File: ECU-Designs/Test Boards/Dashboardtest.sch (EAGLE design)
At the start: 22 parts, among them X2 MINIFIT_5566-6, X3 MINIFIT_5566-10

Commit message: Revisions made courtesy of Nathan.
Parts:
- removed X3: MINIFIT_5566-10, HyTechDevices:MINIFIT_5566-10
- added X1: MINIFIT_5566-8, HyTechDevices:MINIFIT_5566-8
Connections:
- net 20: now also X1-7.S; no longer X3-8.S
- net N$13: now also X1-6.S; no longer X3-6.S
- net N$3: now also X1-1.S; no longer X3-1.S
- net N$5: now also X1-2.S; no longer X3-2.S
- net N$6: now also X1-3.S; no longer X3-3.S
- net N$7: now also X1-4.S; no longer X3-4.S
- net N$8: now also X1-8.S; no longer X3-9.S
- net N$9: now also X1-5.S; no longer X3-5.S
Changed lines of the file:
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@@
 <part name="X2" library="HyTechDevices" deviceset="MINIFIT_5566-6" device=""/>
 <part name="GND6" library="supply1" deviceset="GND" device=""/>
-<part name="X3" library="HyTechDevices" deviceset="MINIFIT_5566-10" device=""/>
 <part name="BUZZER" library="HyTechDevices" deviceset="MINIFIT_5566-2" device=""/>
 <part name="GND7" library="supply1" deviceset="GND" device=""/>
 <part name="GND5" library="supply1" deviceset="GND" device=""/>
+<part name="X1" library="HyTechDevices" deviceset="MINIFIT_5566-8" device=""/>
 </parts>
 <sheets>
@@
 <instance part="X2" gate="-6" x="-27.94" y="10.16" rot="R180"/>
 <instance part="GND6" gate="1" x="-17.78" y="10.16" rot="R90"/>
-<instance part="X3" gate="-1" x="15.24" y="53.34" rot="R90"/>
-<instance part="X3" gate="-2" x="17.78" y="53.34" rot="R90"/>
-<instance part="X3" gate="-3" x="20.32" y="53.34" rot="R90"/>
-<instance part="X3" gate="-4" x="22.86" y="53.34" rot="R90"/>
-<instance part="X3" gate="-5" x="25.4" y="53.34" rot="R90"/>
-<instance part="X3" gate="-6" x="27.94" y="53.34" rot="R90"/>
-<instance part="X3" gate="-7" x="30.48" y="53.34" rot="R90"/>
-<instance part="X3" gate="-8" x="33.02" y="53.34" rot="R90"/>
-<instance part="X3" gate="-9" x="35.56" y="58.42" rot="R90"/>
-<instance part="X3" gate="-10" x="38.1" y="58.42" rot="R90"/>
 <instance part="BUZZER" gate="-2" x="76.2" y="50.8"/>
 <instance part="BUZZER" gate="-1" x="76.2" y="53.34"/>
 <instance part="GND7" gate="1" x="55.88" y="40.64" rot="R180"/>
 <instance part="GND5" gate="1" x="48.26" y="-25.4"/>
+<instance part="X1" gate="-1" x="15.24" y="63.5" rot="R90"/>
+<instance part="X1" gate="-2" x="17.78" y="63.5" rot="R90"/>
+<instance part="X1" gate="-3" x="20.32" y="63.5" rot="R90"/>
+<instance part="X1" gate="-4" x="22.86" y="63.5" rot="R90"/>
+<instance part="X1" gate="-5" x="25.4" y="63.5" rot="R90"/>
+<instance part="X1" gate="-6" x="27.94" y="63.5" rot="R90"/>
+<instance part="X1" gate="-7" x="30.48" y="63.5" rot="R90"/>
+<instance part="X1" gate="-8" x="33.02" y="63.5" rot="R90"/>
 </instances>
 <busses>
@@
 <wire x1="-5.08" y1="35.56" x2="-5.08" y2="43.18" width="0.1524" layer="91"/>
 <wire x1="-5.08" y1="43.18" x2="15.24" y2="43.18" width="0.1524" layer="91"/>
-<wire x1="15.24" y1="43.18" x2="15.24" y2="50.8" width="0.1524" layer="91"/>
-<pinref part="X3" gate="-1" pin="S"/>
+<pinref part="X1" gate="-1" pin="S"/>
+<wire x1="15.24" y1="43.18" x2="15.24" y2="60.96" width="0.1524" layer="91"/>
 </segment>
 </net>
@@
 <wire x1="5.08" y1="35.56" x2="5.08" y2="40.64" width="0.1524" layer="91"/>
 <wire x1="5.08" y1="40.64" x2="17.78" y2="40.64" width="0.1524" layer="91"/>
-<wire x1="17.78" y1="40.64" x2="17.78" y2="50.8" width="0.1524" layer="91"/>
-<pinref part="X3" gate="-2" pin="S"/>
+<pinref part="X1" gate="-2" pin="S"/>
+<wire x1="17.78" y1="60.96" x2="17.78" y2="40.64" width="0.1524" layer="91"/>
 </segment>
 </net>
@@
 <wire x1="15.24" y1="35.56" x2="15.24" y2="38.1" width="0.1524" layer="91"/>
 <wire x1="15.24" y1="38.1" x2="20.32" y2="38.1" width="0.1524" layer="91"/>
-<wire x1="20.32" y1="38.1" x2="20.32" y2="50.8" width="0.1524" layer="91"/>
-<pinref part="X3" gate="-3" pin="S"/>
+<wire x1="20.32" y1="38.1" x2="20.32" y2="60.96" width="0.1524" layer="91"/>
+<pinref part="X1" gate="-3" pin="S"/>
 </segment>
 </net>
@@
 <wire x1="25.4" y1="35.56" x2="25.4" y2="38.1" width="0.1524" layer="91"/>
 <wire x1="25.4" y1="38.1" x2="22.86" y2="38.1" width="0.1524" layer="91"/>
-<wire x1="22.86" y1="38.1" x2="22.86" y2="50.8" width="0.1524" layer="91"/>
-<pinref part="X3" gate="-4" pin="S"/>
+<wire x1="22.86" y1="38.1" x2="22.86" y2="60.96" width="0.1524" layer="91"/>
+<pinref part="X1" gate="-4" pin="S"/>
 </segment>
 </net>
@@
 <wire x1="35.56" y1="35.56" x2="35.56" y2="40.64" width="0.1524" layer="91"/>
 <wire x1="35.56" y1="40.64" x2="25.4" y2="40.64" width="0.1524" layer="91"/>
-<wire x1="25.4" y1="40.64" x2="25.4" y2="50.8" width="0.1524" layer="91"/>
-<pinref part="X3" gate="-5" pin="S"/>
+<pinref part="X1" gate="-5" pin="S"/>
+<wire x1="25.4" y1="60.96" x2="25.4" y2="40.64" width="0.1524" layer="91"/>
 </segment>
 </net>
@@
 <wire x1="45.72" y1="35.56" x2="45.72" y2="43.18" width="0.1524" layer="91"/>
 <wire x1="45.72" y1="43.18" x2="27.94" y2="43.18" width="0.1524" layer="91"/>
-<wire x1="27.94" y1="43.18" x2="27.94" y2="50.8" width="0.1524" layer="91"/>
-<pinref part="X3" gate="-6" pin="S"/>
+<pinref part="X1" gate="-6" pin="S"/>
+<wire x1="27.94" y1="60.96" x2="27.94" y2="43.18" width="0.1524" layer="91"/>
 </segment>
 </net>
@@
 <junction x="15.24" y="12.7"/>
 <wire x1="68.58" y1="12.7" x2="55.88" y2="12.7" width="0.1524" layer="91"/>
-<pinref part="X3" gate="-8" pin="S"/>
 <wire x1="33.02" y1="50.8" x2="33.02" y2="48.26" width="0.1524" layer="91"/>
 <pinref part="BUZZER" gate="-2" pin="S"/>
@@
 <wire x1="68.58" y1="50.8" x2="68.58" y2="48.26" width="0.1524" layer="91"/>
 <junction x="68.58" y="48.26"/>
+<wire x1="33.02" y1="50.8" x2="30.48" y2="50.8" width="0.1524" layer="91"/>
+<pinref part="X1" gate="-7" pin="S"/>
+<wire x1="30.48" y1="50.8" x2="30.48" y2="60.96" width="0.1524" layer="91"/>
 </segment>
 </net>
 <net name="N$8" class="0">
 <segment>
-<pinref part="X3" gate="-9" pin="S"/>
 <wire x1="35.56" y1="55.88" x2="35.56" y2="50.8" width="0.1524" layer="91"/>
 <wire x1="35.56" y1="50.8" x2="66.04" y2="50.8" width="0.1524" layer="91"/>
@@
 <pinref part="BUZZER" gate="-1" pin="S"/>
 <wire x1="66.04" y1="53.34" x2="73.66" y2="53.34" width="0.1524" layer="91"/>
-</segment>
-</net>
+<pinref part="X1" gate="-8" pin="S"/>
+<wire x1="35.56" y1="55.88" x2="33.02" y2="55.88" width="0.1524" layer="91"/>
+<wire x1="33.02" y1="55.88" x2="33.02" y2="60.96" width="0.1524" layer="91"/>
+</segment>
+</net>

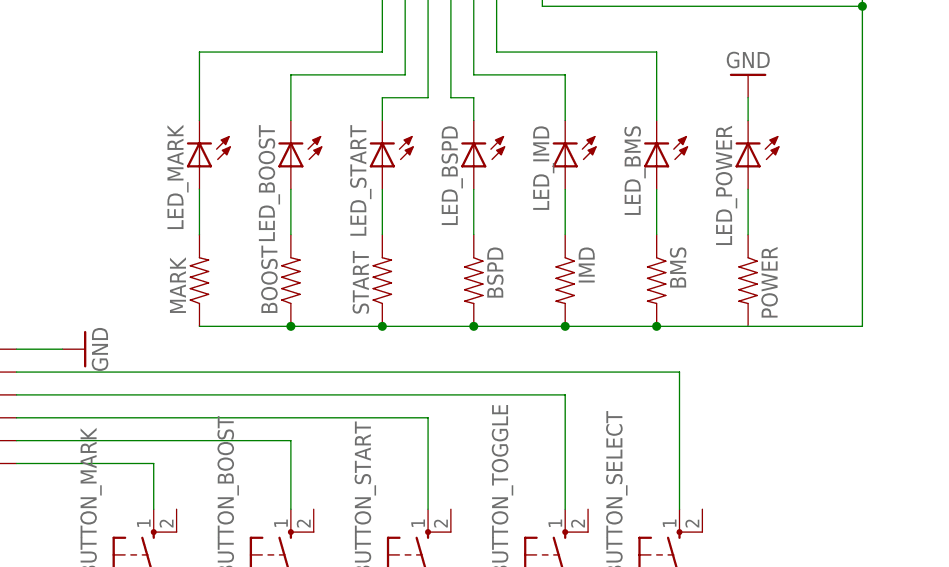
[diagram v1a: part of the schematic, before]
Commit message: added resistor values
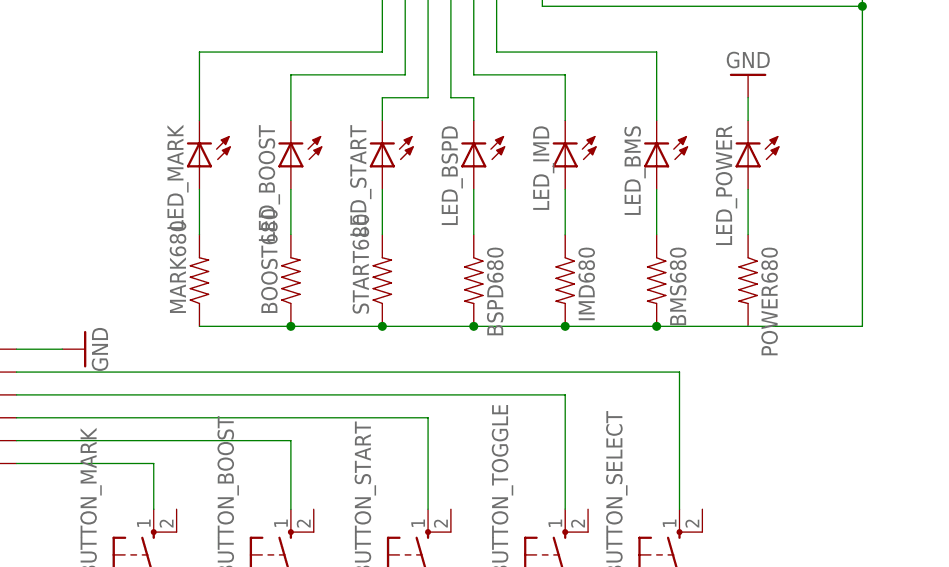
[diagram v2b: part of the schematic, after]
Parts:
- renumbered BMS to BMS680, BOOST to BOOST680, BSPD to BSPD680, IMD to IMD680, MARK to MARK680, POWER to POWER680, START to START680
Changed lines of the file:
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@@
 <part name="LED_POWER" library="HyTechDevices" deviceset="LED" device="-5MM"/>
 <part name="LED_BMS" library="HyTechDevices" deviceset="LED" device="-5MM"/>
-<part name="POWER" library="HyTechDevices" deviceset="RESISTOR" device="EZ"/>
-<part name="BMS" library="HyTechDevices" deviceset="RESISTOR" device="EZ"/>
-<part name="IMD" library="HyTechDevices" deviceset="RESISTOR" device="EZ"/>
-<part name="BSPD" library="HyTechDevices" deviceset="RESISTOR" device="EZ"/>
+<part name="POWER680" library="HyTechDevices" deviceset="RESISTOR" device="EZ"/>
+<part name="BMS680" library="HyTechDevices" deviceset="RESISTOR" device="EZ"/>
+<part name="IMD680" library="HyTechDevices" deviceset="RESISTOR" device="EZ"/>
+<part name="BSPD680" library="HyTechDevices" deviceset="RESISTOR" device="EZ"/>
 <part name="LED_MARK" library="HyTechDevices" deviceset="LED" device="-5MM"/>
 <part name="LED_BOOST" library="HyTechDevices" deviceset="LED" device="-5MM"/>
 <part name="LED_START" library="HyTechDevices" deviceset="LED" device="-5MM"/>
-<part name="MARK" library="HyTechDevices" deviceset="RESISTOR" device="EZ"/>
-<part name="BOOST" library="HyTechDevices" deviceset="RESISTOR" device="EZ"/>
-<part name="START" library="HyTechDevices" deviceset="RESISTOR" device="EZ"/>
+<part name="MARK680" library="HyTechDevices" deviceset="RESISTOR" device="EZ"/>
+<part name="BOOST680" library="HyTechDevices" deviceset="RESISTOR" device="EZ"/>
+<part name="START680" library="HyTechDevices" deviceset="RESISTOR" device="EZ"/>
 <part name="GND1" library="supply1" deviceset="GND" device=""/>
 <part name="GND2" library="supply1" deviceset="GND" device=""/>
@@
 <instance part="LED_POWER" gate="LED" x="55.88" y="30.48" rot="R180"/>
 <instance part="LED_BMS" gate="LED" x="45.72" y="30.48" rot="R180"/>
-<instance part="POWER" gate="G$1" x="55.88" y="17.78" rot="R270"/>
-<instance part="BMS" gate="G$1" x="45.72" y="17.78" rot="R270"/>
-<instance part="IMD" gate="G$1" x="35.56" y="17.78" rot="R270"/>
-<instance part="BSPD" gate="G$1" x="25.4" y="17.78" rot="R270"/>
+<instance part="POWER680" gate="G$1" x="55.88" y="17.78" rot="R270"/>
+<instance part="BMS680" gate="G$1" x="45.72" y="17.78" rot="R270"/>
+<instance part="IMD680" gate="G$1" x="35.56" y="17.78" rot="R270"/>
+<instance part="BSPD680" gate="G$1" x="25.4" y="17.78" rot="R270"/>
 <instance part="LED_MARK" gate="LED" x="-5.08" y="30.48" rot="R180"/>
 <instance part="LED_BOOST" gate="LED" x="5.08" y="30.48" rot="R180"/>
 <instance part="LED_START" gate="LED" x="15.24" y="30.48" rot="R180"/>
-<instance part="MARK" gate="G$1" x="-5.08" y="17.78" rot="R90"/>
-<instance part="BOOST" gate="G$1" x="5.08" y="17.78" rot="R90"/>
-<instance part="START" gate="G$1" x="15.24" y="17.78" rot="R90"/>
+<instance part="MARK680" gate="G$1" x="-5.08" y="17.78" rot="R90"/>
+<instance part="BOOST680" gate="G$1" x="5.08" y="17.78" rot="R90"/>
+<instance part="START680" gate="G$1" x="15.24" y="17.78" rot="R90"/>
 <instance part="GND1" gate="1" x="-10.16" y="-25.4"/>
 <instance part="GND2" gate="1" x="5.08" y="-25.4"/>
@@
 <net name="N$1" class="0">
 <segment>
-<pinref part="POWER" gate="G$1" pin="1"/>
+<pinref part="POWER680" gate="G$1" pin="1"/>
 <pinref part="LED_POWER" gate="LED" pin="A"/>
 <wire x1="55.88" y1="22.86" x2="55.88" y2="27.94" width="0.1524" layer="91"/>
@@
 <net name="N$2" class="0">
 <segment>
-<pinref part="BMS" gate="G$1" pin="1"/>
+<pinref part="BMS680" gate="G$1" pin="1"/>
 <pinref part="LED_BMS" gate="LED" pin="A"/>
 <wire x1="45.72" y1="22.86" x2="45.72" y2="27.94" width="0.1524" layer="91"/>
@@
 <net name="LED_IMD" class="0">
 <segment>
-<pinref part="IMD" gate="G$1" pin="1"/>
+<pinref part="IMD680" gate="G$1" pin="1"/>
 <pinref part="LED_IMD" gate="LED" pin="A"/>
 <wire x1="35.56" y1="22.86" x2="35.56" y2="27.94" width="0.1524" layer="91"/>
@@
 <net name="N$4" class="0">
 <segment>
-<pinref part="BSPD" gate="G$1" pin="1"/>
+<pinref part="BSPD680" gate="G$1" pin="1"/>
 <pinref part="LED_BSPD" gate="LED" pin="A"/>
 <wire x1="25.4" y1="22.86" x2="25.4" y2="27.94" width="0.1524" layer="91"/>
@@
 <segment>
 <pinref part="LED_MARK" gate="LED" pin="A"/>
-<pinref part="MARK" gate="G$1" pin="2"/>
+<pinref part="MARK680" gate="G$1" pin="2"/>
 <wire x1="-5.08" y1="27.94" x2="-5.08" y2="22.86" width="0.1524" layer="91"/>
 </segment>
@@
 <segment>
 <pinref part="LED_BOOST" gate="LED" pin="A"/>
-<pinref part="BOOST" gate="G$1" pin="2"/>
+<pinref part="BOOST680" gate="G$1" pin="2"/>
 <wire x1="5.08" y1="27.94" x2="5.08" y2="22.86" width="0.1524" layer="91"/>
 </segment>
@@
 <segment>
 <pinref part="LED_START" gate="LED" pin="A"/>
-<pinref part="START" gate="G$1" pin="2"/>
+<pinref part="START680" gate="G$1" pin="2"/>
 <wire x1="15.24" y1="27.94" x2="15.24" y2="22.86" width="0.1524" layer="91"/>
 </segment>
@@
 <wire x1="33.02" y1="48.26" x2="68.58" y2="48.26" width="0.1524" layer="91"/>
 <wire x1="68.58" y1="48.26" x2="68.58" y2="12.7" width="0.1524" layer="91"/>
-<pinref part="POWER" gate="G$1" pin="2"/>
-<pinref part="BMS" gate="G$1" pin="2"/>
+<pinref part="POWER680" gate="G$1" pin="2"/>
+<pinref part="BMS680" gate="G$1" pin="2"/>
 <wire x1="55.88" y1="12.7" x2="45.72" y2="12.7" width="0.1524" layer="91"/>
-<pinref part="IMD" gate="G$1" pin="2"/>
+<pinref part="IMD680" gate="G$1" pin="2"/>
 <wire x1="45.72" y1="12.7" x2="35.56" y2="12.7" width="0.1524" layer="91"/>
 <junction x="45.72" y="12.7"/>
-<pinref part="BSPD" gate="G$1" pin="2"/>
+<pinref part="BSPD680" gate="G$1" pin="2"/>
 <wire x1="35.56" y1="12.7" x2="25.4" y2="12.7" width="0.1524" layer="91"/>
 <junction x="35.56" y="12.7"/>
-<pinref part="MARK" gate="G$1" pin="1"/>
-<pinref part="BOOST" gate="G$1" pin="1"/>
+<pinref part="MARK680" gate="G$1" pin="1"/>
+<pinref part="BOOST680" gate="G$1" pin="1"/>
 <wire x1="-5.08" y1="12.7" x2="5.08" y2="12.7" width="0.1524" layer="91"/>
-<pinref part="START" gate="G$1" pin="1"/>
+<pinref part="START680" gate="G$1" pin="1"/>
 <wire x1="5.08" y1="12.7" x2="15.24" y2="12.7" width="0.1524" layer="91"/>
 <junction x="5.08" y="12.7"/>
